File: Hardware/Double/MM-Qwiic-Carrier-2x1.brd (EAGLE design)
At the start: 80 x 35.6 mm, 89 parts, among them J15 MICROMOD-2222-C, J2 QWIIC_RIGHT_ANGLE, J5 Vertical Qwiic Connector, U1 MCP73831, U5 AP7361C-33FGEUDFN-8

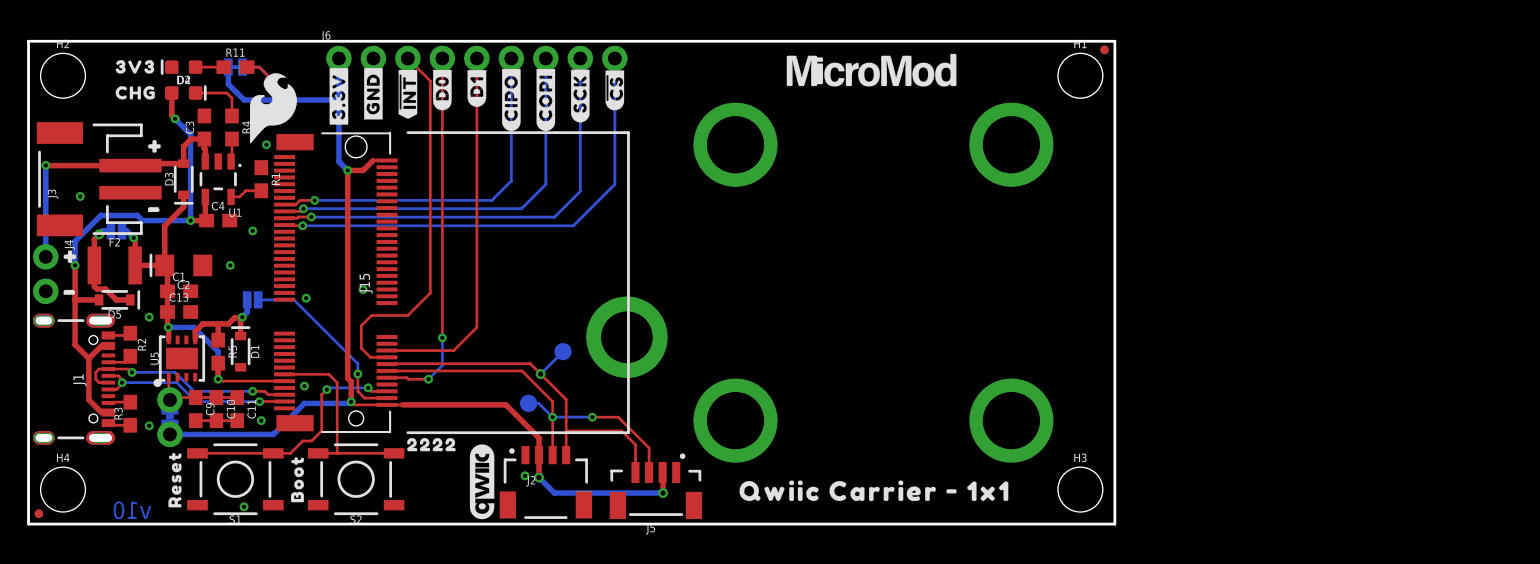
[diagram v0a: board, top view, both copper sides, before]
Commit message: Renaming
1x1 --> Single
2x1 --> Double
Re-panelized
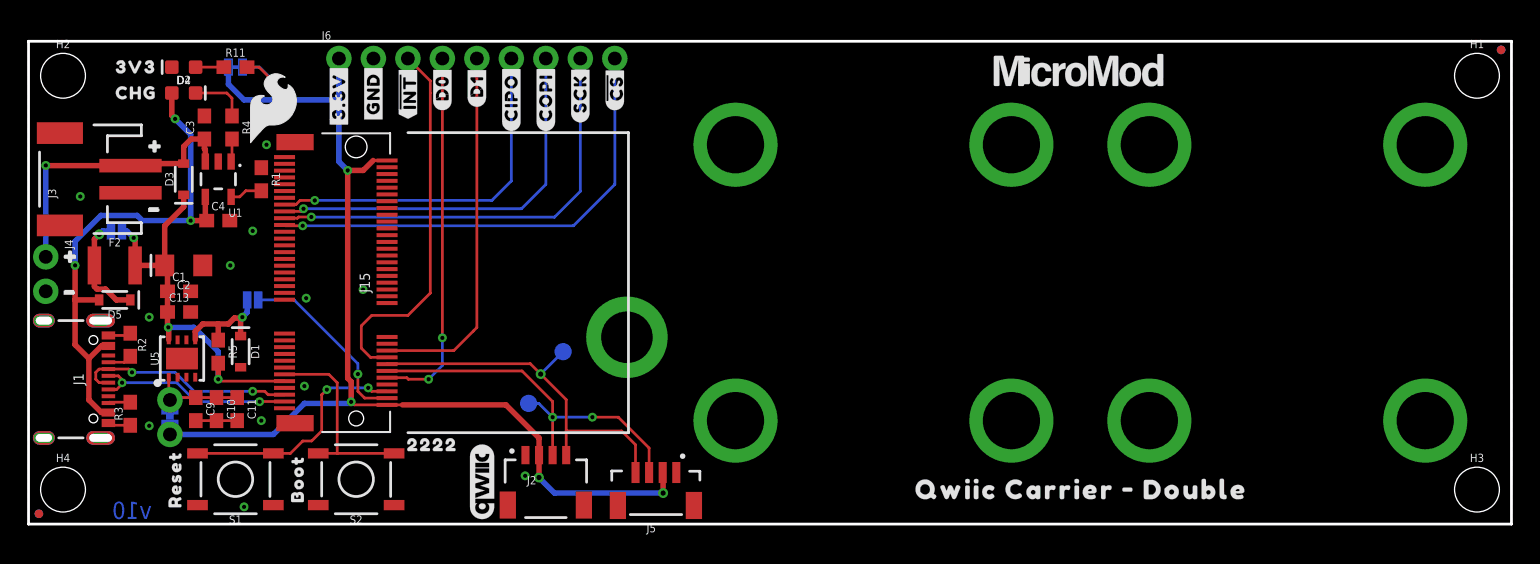
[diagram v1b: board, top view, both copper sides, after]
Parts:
- added U$2: QWIIC_BOARD_OUTLINESTANDOFF, SparkFun-Boards:QWIIC_BOARD_MOUNT_SMD_STANDOFFS
- U$10, U$13: device output:QWIIC_CARRIER_#_1X10 -> output:QWIIC_CARRIER_#_DOUBLE0
- moved H1 29.2 mm to (106.7, 33.0)
- moved H3 29.2 mm to (106.7, 2.54)
- moved FD2 29.2 mm to (108.5, 34.9)
- moved FD4 29.2 mm to (108.5, 34.9)
- moved U$67 15.2 mm to (77.3, 33.4)
- moved U$10 13.0 mm to (64.3, 2.54)
- moved U$13 2.50 mm to (45.0, 17.7)
- moved LOGO1 0.64 mm to (31.8, 22.2)
- moved U$68 0.63 mm to (31.8, 19.7)
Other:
- board size 80 x 35.6 mm -> 109.2 x 35.6 mm
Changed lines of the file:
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@@
 <layer number="45" name="Holes" color="7" fill="1" visible="yes" active="yes"/>
 <layer number="46" name="Milling" color="3" fill="1" visible="no" active="yes"/>
-<layer number="47" name="Measures" color="7" fill="1" visible="no" active="yes"/>
+<layer number="47" name="Measures" color="7" fill="1" visible="yes" active="yes"/>
 <layer number="48" name="Document" color="7" fill="1" visible="no" active="yes"/>
 <layer number="49" name="Reference" color="7" fill="1" visible="no" active="yes"/>
@@
 <plain>
 <wire x1="0" y1="0" x2="0" y2="35.56" width="0.2032" layer="20"/>
-<wire x1="0" y1="35.56" x2="80.01" y2="35.56" width="0.2032" layer="20"/>
-<wire x1="80.01" y1="35.56" x2="80.01" y2="0" width="0.2032" layer="20"/>
-<wire x1="80.01" y1="0" x2="0" y2="0" width="0.2032" layer="20"/>
+<wire x1="0" y1="35.56" x2="109.22" y2="35.56" width="0.2032" layer="20"/>
+<wire x1="109.22" y1="35.56" x2="109.22" y2="0" width="0.2032" layer="20"/>
+<wire x1="109.22" y1="0" x2="0" y2="0" width="0.2032" layer="20"/>
 <text x="7.62" y="1.016" size="1.27" layer="16" font="vector" ratio="20" rot="MR180" align="center">v10</text>
 <wire x1="27.94" y1="28.829" x2="44.185" y2="28.829" width="0.2032" layer="21"/>
@@
 <wire x1="44.185" y1="6.731" x2="27.94" y2="6.731" width="0.2032" layer="21"/>
 <text x="36.83" y="-21.59" size="1.778" layer="51" font="vector" ratio="15">Priyanka Makin</text>
-<dimension x1="0" y1="35.56" x2="80.01" y2="35.56" x3="40.005" y3="45.72" textsize="1.778" textratio="15" layer="47" unit="inch"/>
-<dimension x1="80.01" y1="35.56" x2="80.01" y2="0" x3="91.44" y3="17.78" textsize="1.778" textratio="15" layer="47" unit="inch"/>
-<text x="43.434" y="42.418" size="1.778" layer="47" font="vector" ratio="15">in</text>
-<text x="85.344" y="23.241" size="1.778" layer="47" font="vector" ratio="15" rot="R270">in</text>
-<dimension x1="2.54" y1="33.02" x2="77.47" y2="33.02" x3="40.005" y3="41.91" textsize="1.778" textratio="15" layer="47" unit="inch"/>
-<dimension x1="77.47" y1="33.02" x2="77.47" y2="2.54" x3="87.63" y3="17.78" textsize="1.778" textratio="15" layer="47" unit="inch"/>
-<text x="43.434" y="46.228" size="1.778" layer="47" font="vector" ratio="15">in</text>
-<text x="89.154" y="23.241" size="1.778" layer="47" font="vector" ratio="15" rot="R270">in</text>
+<text x="58.674" y="42.418" size="1.778" layer="47" font="vector" ratio="15">in</text>
+<text x="114.554" y="23.241" size="1.778" layer="47" font="vector" ratio="15" rot="R270">in</text>
+<text x="57.404" y="46.228" size="1.778" layer="47" font="vector" ratio="15">in</text>
+<text x="118.364" y="23.241" size="1.778" layer="47" font="vector" ratio="15" rot="R270">in</text>
 <dimension x1="52.07" y1="27.94" x2="72.39" y2="27.94" x3="62.23" y3="38.1" textsize="1.778" textratio="15" layer="47" unit="inch"/>
-<dimension x1="72.39" y1="27.94" x2="72.39" y2="7.62" x3="83.82" y3="17.78" textsize="1.778" textratio="15" layer="47" unit="inch"/>
-<text x="81.534" y="23.241" size="1.778" layer="47" font="vector" ratio="15" rot="R270">in</text>
+<text x="110.744" y="23.241" size="1.778" layer="47" font="vector" ratio="15" rot="R270">in</text>
 <text x="65.024" y="38.608" size="1.778" layer="47" font="vector" ratio="15">in</text>
+<dimension x1="2.54" y1="33.02" x2="106.68" y2="33.02" x3="54.61" y3="41.91" textsize="1.778" textratio="15" layer="47" unit="inch"/>
+<dimension x1="0" y1="35.56" x2="109.22" y2="35.56" x3="54.61" y3="45.72" textsize="1.778" textratio="15" layer="47" unit="inch"/>
+<dimension x1="102.87" y1="27.94" x2="102.87" y2="7.62" x3="113.03" y3="17.78" textsize="1.778" textratio="15" layer="47" unit="inch"/>
+<dimension x1="106.68" y1="33.02" x2="106.68" y2="2.54" x3="116.84" y3="17.78" textsize="1.778" textratio="15" layer="47" unit="inch"/>
+<dimension x1="109.22" y1="35.56" x2="109.22" y2="0" x3="120.65" y3="17.78" textsize="1.778" textratio="15" layer="47" unit="inch"/>
+<dimension x1="82.55" y1="27.94" x2="102.87" y2="27.94" x3="92.71" y3="38.1" textsize="1.778" textratio="15" layer="47" unit="inch"/>
+<text x="95.504" y="38.608" size="1.778" layer="47" font="vector" ratio="15">in</text>
 </plain>
 <attributes>
@@
 </element>
 <element name="FD1" library="SparkFun-Aesthetics" package="FIDUCIAL-MICRO" value="FIDUCIALUFIDUCIAL" x="0.762" y="0.762" smashed="yes"/>
-<element name="FD2" library="SparkFun-Aesthetics" package="FIDUCIAL-MICRO" value="FIDUCIALUFIDUCIAL" x="79.248" y="34.925" smashed="yes"/>
+<element name="FD2" library="SparkFun-Aesthetics" package="FIDUCIAL-MICRO" value="FIDUCIALUFIDUCIAL" x="108.458" y="34.925" smashed="yes"/>
 <element name="FD3" library="SparkFun-Aesthetics" package="FIDUCIAL-MICRO" value="FIDUCIALUFIDUCIAL" x="0.762" y="0.762" smashed="yes" rot="MR0"/>
-<element name="FD4" library="SparkFun-Aesthetics" package="FIDUCIAL-MICRO" value="FIDUCIALUFIDUCIAL" x="79.248" y="34.925" smashed="yes" rot="MR0"/>
-<element name="H1" library="SparkFun-Hardware" package="STAND-OFF" value="STAND-OFF" x="77.47" y="33.02" smashed="yes">
-<attribute name="NAME" x="77.47" y="35.052" size="0.6096" layer="25" font="vector" ratio="20" align="bottom-center"/>
-<attribute name="VALUE" x="77.47" y="30.988" size="0.6096" layer="27" font="vector" ratio="20" align="top-center"/>
+<element name="FD4" library="SparkFun-Aesthetics" package="FIDUCIAL-MICRO" value="FIDUCIALUFIDUCIAL" x="108.458" y="34.925" smashed="yes" rot="MR0"/>
+<element name="H1" library="SparkFun-Hardware" package="STAND-OFF" value="STAND-OFF" x="106.68" y="33.02" smashed="yes">
+<attribute name="NAME" x="106.68" y="35.052" size="0.6096" layer="25" font="vector" ratio="20" align="bottom-center"/>
+<attribute name="VALUE" x="106.68" y="30.988" size="0.6096" layer="27" font="vector" ratio="20" align="top-center"/>
 </element>
 <element name="H2" library="SparkFun-Hardware" package="STAND-OFF" value="STAND-OFF" x="2.54" y="33.02" smashed="yes">
@@
 <attribute name="VALUE" x="2.54" y="30.988" size="0.6096" layer="27" font="vector" ratio="20" align="top-center"/>
 </element>
-<element name="H3" library="SparkFun-Hardware" package="STAND-OFF" value="STAND-OFF" x="77.47" y="2.54" smashed="yes">
-<attribute name="NAME" x="77.47" y="4.572" size="0.6096" layer="25" font="vector" ratio="20" align="bottom-center"/>
-<attribute name="VALUE" x="77.47" y="0.508" size="0.6096" layer="27" font="vector" ratio="20" align="top-center"/>
+<element name="H3" library="SparkFun-Hardware" package="STAND-OFF" value="STAND-OFF" x="106.68" y="2.54" smashed="yes">
+<attribute name="NAME" x="106.68" y="4.572" size="0.6096" layer="25" font="vector" ratio="20" align="bottom-center"/>
+<attribute name="VALUE" x="106.68" y="0.508" size="0.6096" layer="27" font="vector" ratio="20" align="top-center"/>
 </element>
 <element name="H4" library="SparkFun-Hardware" package="STAND-OFF" value="STAND-OFF" x="2.54" y="2.54" smashed="yes">
@@
 <attribute name="VALUE" x="23.495" y="17.78" size="0.762" layer="27" rot="R270" align="center"/>
 </element>
-<element name="LOGO1" library="SparkFun-Aesthetics" package="SFE_LOGO_NAME_FLAME_.2" value="SFE_LOGO_NAME_FLAME.2_INCH" x="31.75" y="21.59" smashed="yes" rot="MR0"/>
+<element name="LOGO1" library="SparkFun-Aesthetics" package="SFE_LOGO_NAME_FLAME_.2" value="SFE_LOGO_NAME_FLAME.2_INCH" x="31.75" y="22.225" smashed="yes" rot="MR0"/>
 <element name="U$44" library="SparkFun-Aesthetics" package="SFE_LOGO_FLAME_.2" value="" x="18.034" y="30.607" smashed="yes"/>
-<element name="U$67" library="SparkFun-MicroMod" package="MICROMOD_LOGO_.5" value="" x="62.103" y="33.401" smashed="yes"/>
-<element name="U$68" library="SparkFun-MicroMod" package="MICROMOD_LOGO_.5" value="" x="31.75" y="19.05" smashed="yes" rot="MR0"/>
+<element name="U$67" library="SparkFun-MicroMod" package="MICROMOD_LOGO_.5" value="" x="77.343" y="33.401" smashed="yes"/>
+<element name="U$68" library="SparkFun-MicroMod" package="MICROMOD_LOGO_.5" value="" x="31.75" y="19.685" smashed="yes" rot="MR0"/>
 <element name="J2" library="SparkFun-Connectors" package="JST04_1MM_RA" value="QWIIC_RIGHT_ANGLE" x="38.1" y="5.08" smashed="yes">
 <attribute name="NAME" x="36.703" y="2.921" size="0.6096" layer="25" font="vector" ratio="20"/>
@@
 </element>
 <element name="U$5" library="SparkFun-Boards" package="QWIIC_BOARD_MOUNT_SMD_STANDOFFS" value="QWIIC_BOARD_OUTLINESTANDOFF" x="62.23" y="17.78" smashed="yes"/>
-<element name="U$10" library="output" package="QWIIC_CARRIER_#_1X10" value="" x="51.308" y="2.413" smashed="yes"/>
-<element name="U$13" library="output" package="QWIIC_CARRIER_#_1X10" value="" x="42.672" y="16.637" smashed="yes" rot="MR0"/>
 <element name="U$3" library="output" package="3V30" value="" x="5.715" y="33.655" smashed="yes"/>
 <element name="U$1" library="output" package="#3#3V_EN#0" value="" x="15.748" y="16.51" smashed="yes" rot="MR0"/>
@@
 <element name="U$15" library="output" package="##INT##0" value="" x="27.94" y="29.845" smashed="yes" rot="R90"/>
 <element name="U$16" library="output" package="##INT##0" value="" x="27.94" y="29.845" smashed="yes" rot="MR90"/>
+<element name="U$2" library="SparkFun-Boards" package="QWIIC_BOARD_MOUNT_SMD_STANDOFFS" value="QWIIC_BOARD_OUTLINESTANDOFF" x="92.71" y="17.78" smashed="yes"/>
+<element name="U$10" library="output" package="QWIIC_CARRIER_#_DOUBLE0" value="" x="64.262" y="2.54" smashed="yes"/>
+<element name="U$13" library="output" package="QWIIC_CARRIER_#_DOUBLE0" value="" x="44.958" y="17.653" smashed="yes" rot="MR0"/>
 </elements>
 <signals>
@@
 <vertex x="0" y="35.56"/>
 <vertex x="0" y="0"/>
-<vertex x="80.01" y="0"/>
-<vertex x="80.01" y="35.56"/>
+<vertex x="109.22" y="0"/>
+<vertex x="109.22" y="35.56"/>
 </polygon>
 <polygon width="0.2032" layer="16" isolate="0.2032">
 <vertex x="0" y="35.56"/>
 <vertex x="0" y="0"/>
-<vertex x="80.01" y="0"/>
-<vertex x="80.01" y="35.56"/>
+<vertex x="109.22" y="0"/>
+<vertex x="109.22" y="35.56"/>
 </polygon>
 <contactref element="J2" pad="1"/>
